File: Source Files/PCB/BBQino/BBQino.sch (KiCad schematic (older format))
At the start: 0 parts

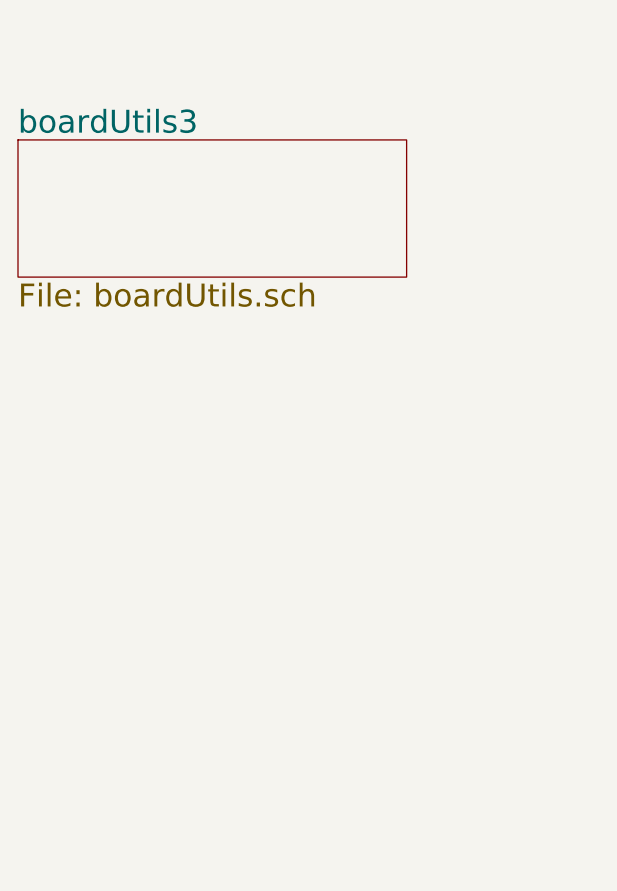
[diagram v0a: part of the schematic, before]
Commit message: Initial dev on power supplies and arduino configuration. PCB skeleton
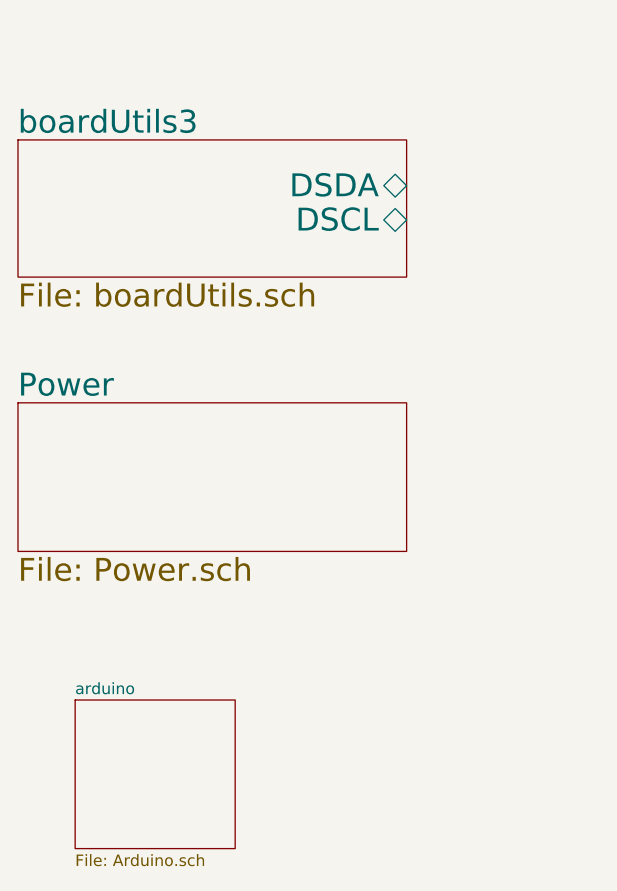
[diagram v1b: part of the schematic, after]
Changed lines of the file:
@@
 $Descr A4 11693 8268
 encoding utf-8
-Sheet 1 2
+Sheet 1 4
 Title "BBQino - DRAFT"
 Date "2021-09-08"
@@
 F0 "boardUtils3" 100
 F1 "boardUtils.sch" 100
+F2 "DSDA" B R 2800 1550 100
+F3 "DSCL" B R 2800 1700 100
+$EndSheet
+$Sheet
+S 1100 2500 1700 650
+U 613C1456
+F0 "Power" 100
+F1 "Power.sch" 100
+$EndSheet
+$Sheet
+S 1350 3800 700  650
+U 613FC6D4
+F0 "arduino" 50
+F1 "Arduino.sch" 50
 $EndSheet
 $EndSCHEMATC
